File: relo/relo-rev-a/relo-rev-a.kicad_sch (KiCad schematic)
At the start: 1 part, among them U1 NA556

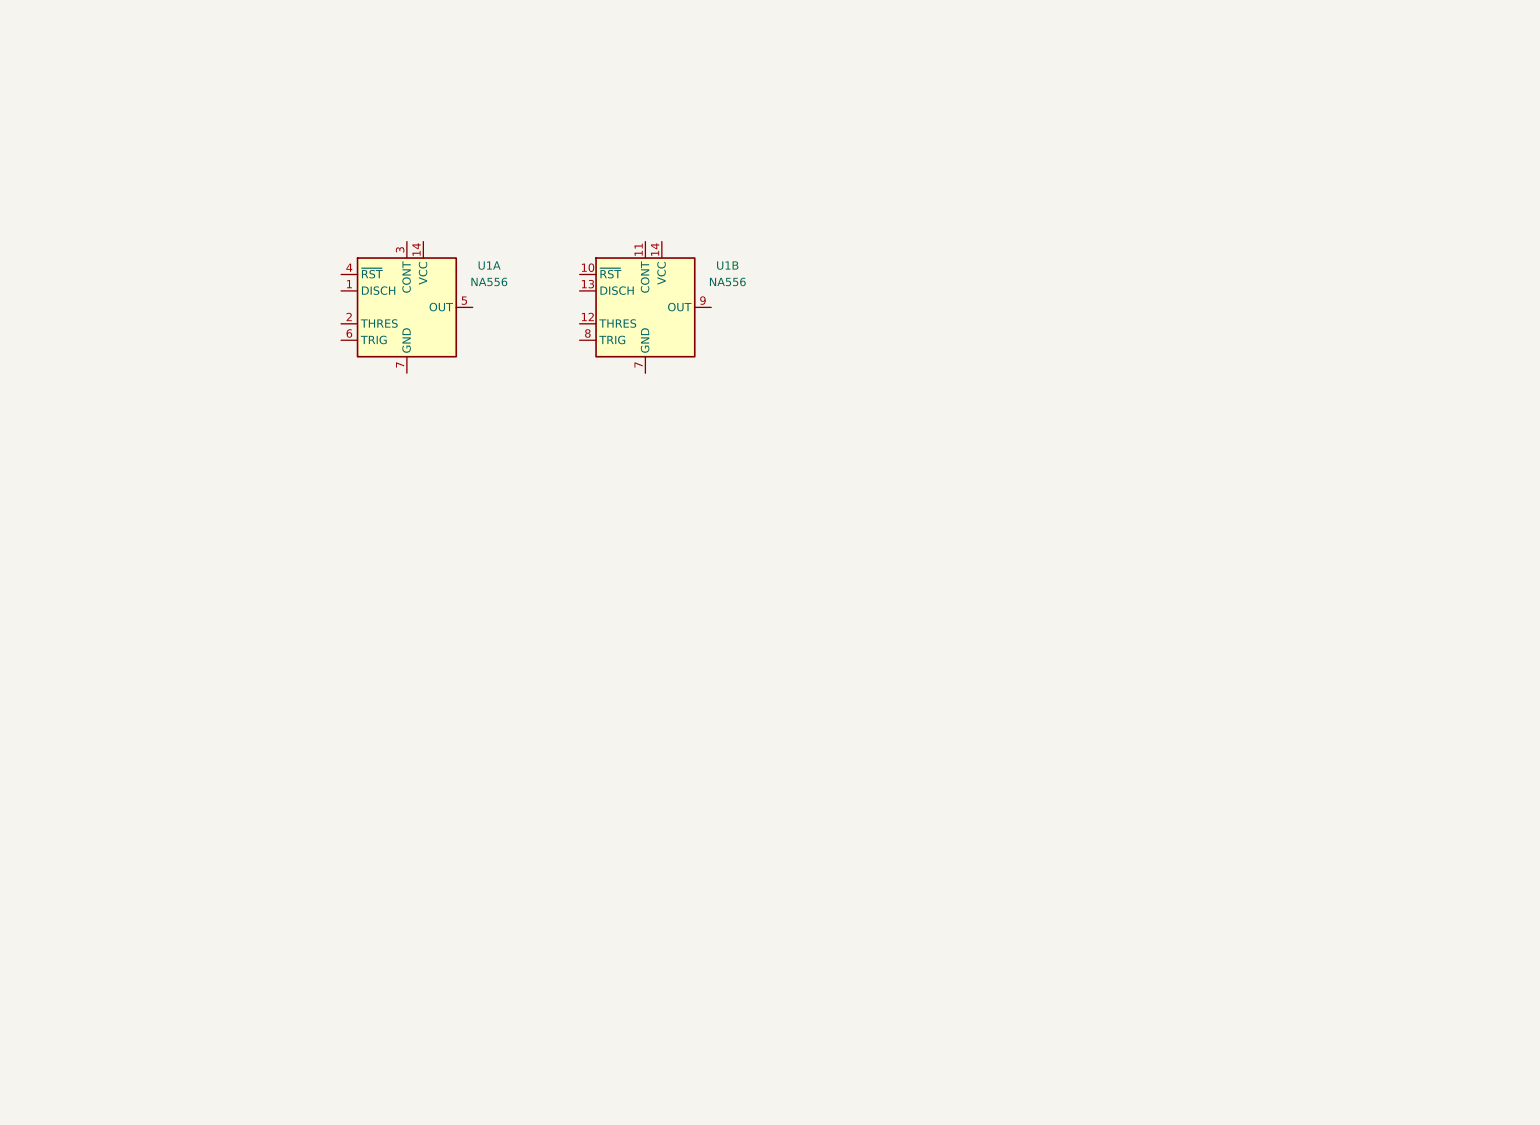
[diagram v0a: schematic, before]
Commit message: agregar relo con 556
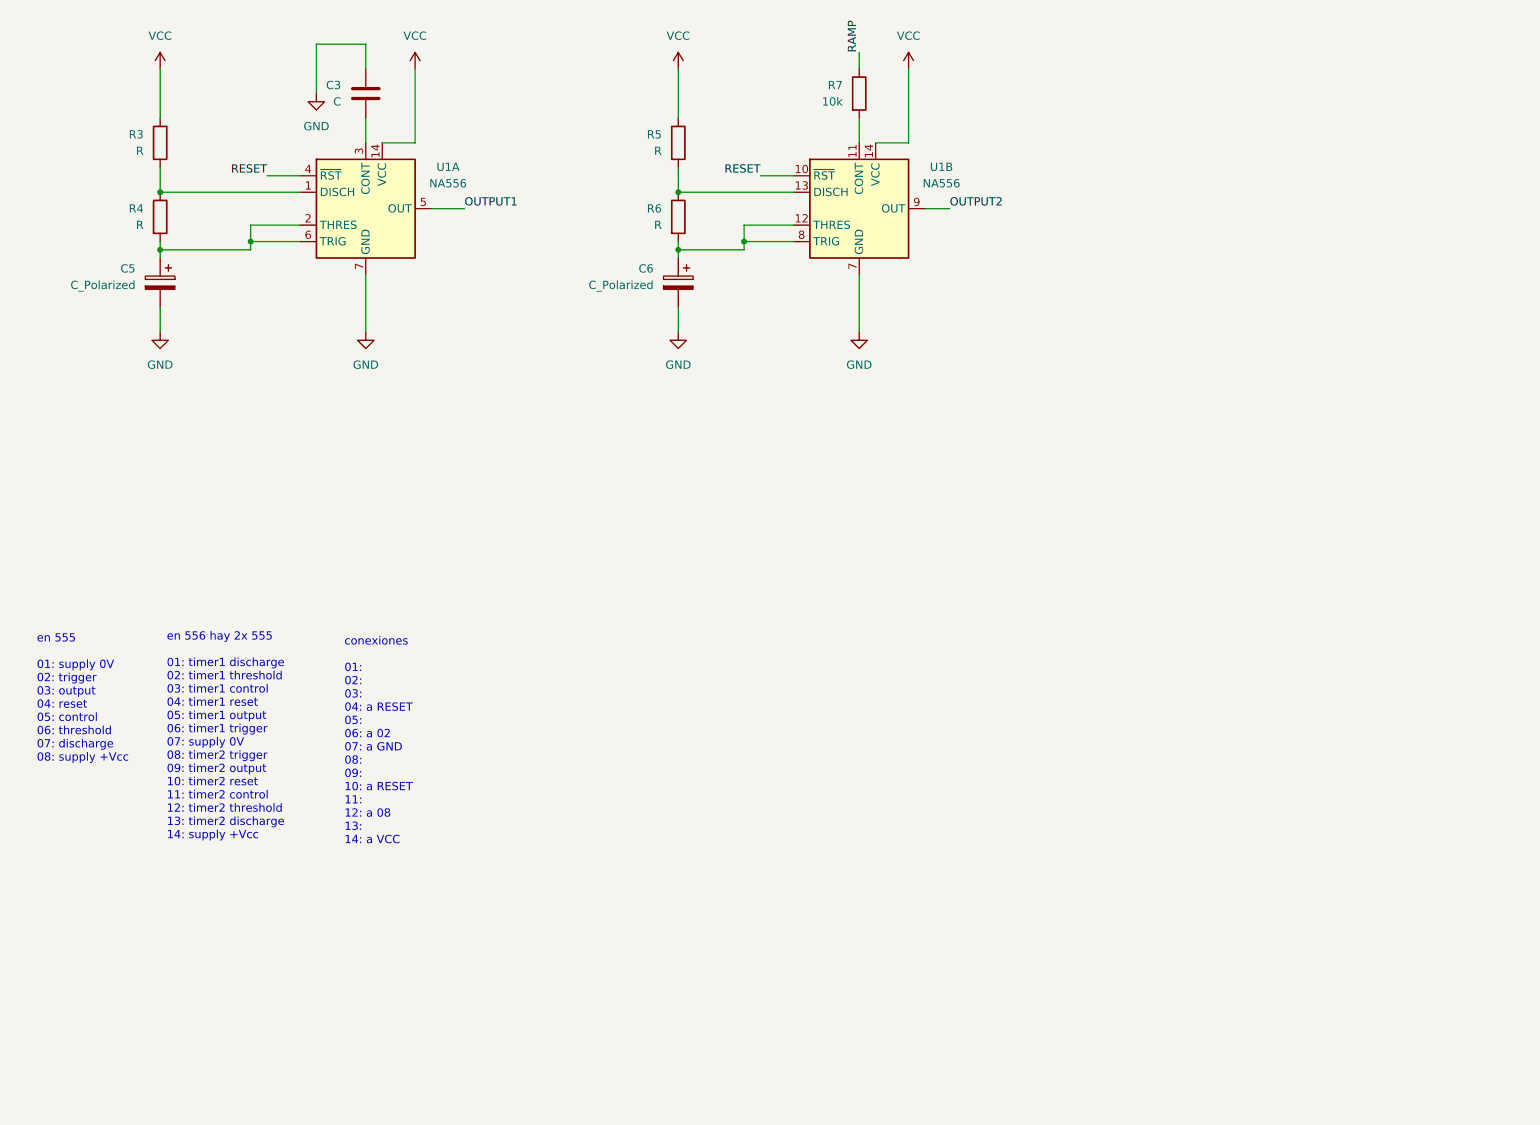
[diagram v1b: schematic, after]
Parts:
- added C3: C, symbol Device:C
- added C5, C6: C_Polarized, symbol Device:C_Polarized
- added R3, R4, R5, R6: R, symbol Device:R
- added R7: 10k, symbol Device:R
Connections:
- net at U1.1 (DISCH): now also R3.2, R4.1
- net VCC: now reaches U1.14 (VCC)
- net VCC: now also U1.14 (VCC), R3.1, R5.1
- net at U1.2 (THRES): now also U1.6 (TRIG), C5.1, R4.2
- net at U1.3 (CONT): now also C3.2
- net RESET: now reaches U1.4 (~{RST})
- net RESET: now also U1.10 (~{RST})
- net OUTPUT1: now reaches U1.5 (OUT)
- net GND: now reaches U1.7 (GND)
- net GND: now also U1.7 (GND), C3.1, C5.2, C6.2
- net at U1.11 (CONT): now also R7.2
- net at U1.12 (THRES): now also U1.8 (TRIG), C6.1, R6.2
- net at U1.13 (DISCH): now also R5.2, R6.1
- net OUTPUT2: now reaches U1.9 (OUT)
- new net RAMP: R7.1
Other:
- note added: "conexiones 01: 02: 03: 04: a RESET 05: 06: a 02 07: a GND 08: 09: 10: a RESET 11: 12: a 08 13: 14: a VCC"
- note added: "en 555 01: supply 0V 02: trigger 03: output 04: reset 05: control 06: threshold 07: discharge 08: supply +Vcc"
- note added: "en 556 hay 2x 555 01: timer1 discharge 02: timer1 threshold 03: timer1 control 04: timer1 reset 05: timer1 output 06: timer1 trigger 07: supply 0V 08: timer2 trigger 09: timer2 output 10: timer2 reset 11: timer2 control 12: timer2 threshold 13: timer2 discharge 14: supply +Vcc"
- moved on the sheet: U1A

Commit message: agregar mas avances en eurorack
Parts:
- removed R7: 10k, symbol Device:R
- added C1, C2: 1u, symbol Device:C_Polarized
- added C4: 100n, symbol Device:C
- added D1, D2: D_Schottky, symbol Device:D_Schottky
- added J1: Conn_02x05_Odd_Even, BYOM_General:IDC-Header_2x05_P2.54mm_Vertical, symbol Connector_Generic:Conn_02x05_Odd_Even
- added J2, J3: AudioJack2_SwitchT, BYOM_General:Jack_3.5mm_QingPu_WQP-PJ398SM_Vertical, symbol Connector_Audio:AudioJack2_SwitchT
- added R1, R2: 1k, symbol Device:R
- added RV1, RV2: 470k, BYOM_General:POT_TH_Alps_RK09K_Single_Vertical, symbol Device:R_Potentiometer
- added U2, U3: TL072, symbol Amplifier_Operational:TL072
- C3: value C -> 100n
- R3, R5: value R -> 10k
- R4, R6: value R -> 100k
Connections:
- net VCC is gone; now on net +12V: R3.1, R5.1, U1.14 (VCC), U1.14 (VCC)
- net GND: now also R4.1, R6.1, C4.1, J1.3 (Pin_3), J1.4 (Pin_4), J1.5 (Pin_5), J1.6 (Pin_6), J1.7 (Pin_7), J1.8 (Pin_8), J2.1, J3.1
- net OUTPUT1: now also R1.1
- net OUTPUT2: now also R2.1
- net at C5.1, U1.2 (THRES), U1.6 (TRIG): now also RV1.3; no longer R4.2
- net at R3.2, U1.1 (DISCH): now also RV1.2; no longer R4.1
- net at U1.11 (CONT): now also C4.2
- net at C6.1, U1.12 (THRES), U1.8 (TRIG): now also RV2.3; no longer R6.2
- net at R5.2, U1.13 (DISCH): now also RV2.2; no longer R6.1
- net RESET renamed +12V
- net +12V: now also D1.1 (K), U2.8 (V+)
- new net: D1.2 (A), J1.10 (Pin_10), J1.9 (Pin_9)
- new net: J3.3, U3.1, U3.2 (-)
- new net: C1.2, R4.2
- new net: C1.1, R1.2, U2.3 (+)
- new net: C2.1, R2.2, U3.3 (+)
- new net: D2.1 (K), J1.1 (Pin_1), J1.2 (Pin_2)
- new net: J2.3, U2.1, U2.2 (-)
- new net: C2.2, R6.2
- new net -12V: D2.2 (A), U2.4 (V-)
- no-connect marks 0 -> 2

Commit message: corregir chip
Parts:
- removed U3: TL072, symbol Amplifier_Operational:TL072
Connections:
- net at J3.3: now also U2.6 (-), U2.7
- net at C2.1, R2.2: now also U2.5 (+)
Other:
- moved on the sheet: U2B
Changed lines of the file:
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@@
-	)
-	(symbol
-		(lib_id "Amplifier_Operational:TL072")
-		(at 185.42 149.86 0)
-		(unit 1)
-		(body_style 1)
-		(exclude_from_sim no)
-		(in_bom yes)
-		(on_board yes)
-		(in_pos_files yes)
-		(dnp no)
-		(fields_autoplaced yes)
-		(property "Reference" "U3"
-			(at 185.42 139.7 0)
-			(show_name no)
-			(do_not_autoplace no)
-			(effects
-				(font
-					(size 1.27 1.27)
-				)
-			)
-		)
-		(property "Value" "TL072"
-			(at 185.42 142.24 0)
-			(show_name no)
-			(do_not_autoplace no)
-			(effects
-				(font
-					(size 1.27 1.27)
-				)
-			)
-		)
-		(property "Footprint" ""
-			(at 185.42 149.86 0)
-			(hide yes)
-			(show_name no)
-			(do_not_autoplace no)
-			(effects
-				(font
-					(size 1.27 1.27)
-				)
-			)
-		)
-		(property "Datasheet" "http://www.ti.com/lit/ds/symlink/tl071.pdf"
-			(at 185.42 149.86 0)
-			(hide yes)
-			(show_name no)
-			(do_not_autoplace no)
-			(effects
-				(font
-					(size 1.27 1.27)
-				)
-			)
-		)
-		(property "Description" "Dual Low-Noise JFET-Input Operational Amplifiers, DIP-8/SOIC-8"
-			(at 185.42 149.86 0)
-			(hide yes)
-			(show_name no)
-			(do_not_autoplace no)
-			(effects
-				(font
-					(size 1.27 1.27)
-				)
-			)
-		)
-		(pin "1"
-		)
-		(pin "4"
-		)
-		(pin "8"
-		)
-		(pin "2"
-		)
-		(pin "3"
-		)
-		(pin "5"
-		)
-		(pin "6"
-		)
-		(pin "7"
-		)
-		(instances
-			(project "relo-rev-a"
-				(path "/47102ddb-7bfb-47a7-a41b-809b4667894a"
-					(reference "U3")
-					(unit 1)
-				)
-			)
-		)
 	)
 	(symbol
@@
 	(symbol
 		(lib_id "Amplifier_Operational:TL072")
-		(at 215.9 72.39 0)
+		(at 185.42 149.86 0)
 		(unit 2)
 		(body_style 1)
@@
 		(fields_autoplaced yes)
 		(property "Reference" "U2"
-			(at 215.9 62.23 0)
+			(at 185.42 139.7 0)
 			(show_name no)
 			(do_not_autoplace no)
@@
 		)
 		(property "Value" "TL072"
-			(at 215.9 64.77 0)
-			(show_name no)
-			(do_not_autoplace no)
-			(effects
-				(font
-					(size 1.27 1.27)
-				)
-			)
-		)
-		(property "Footprint" ""
-			(at 215.9 72.39 0)
+			(at 185.42 142.24 0)
+			(show_name no)
+			(do_not_autoplace no)
+			(effects
+				(font
+					(size 1.27 1.27)
+				)
+			)
+		)
+		(property "Footprint" ""
+			(at 185.42 149.86 0)
 			(hide yes)
 			(show_name no)
@@
 		)
 		(property "Datasheet" "http://www.ti.com/lit/ds/symlink/tl071.pdf"
-			(at 215.9 72.39 0)
+			(at 185.42 149.86 0)
 			(hide yes)
 			(show_name no)
@@
 		)
 		(property "Description" "Dual Low-Noise JFET-Input Operational Amplifiers, DIP-8/SOIC-8"
-			(at 215.9 72.39 0)
-			(hide yes)
-			(show_name no)
+			(at 185.42 149.86 0)
+			(hide yes)
+			(show_name no)
